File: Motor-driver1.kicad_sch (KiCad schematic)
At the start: 46 parts, among them J8 PINHD_1x4_Male, J9 PINHD_1x4_Male, U2 DRV8825PWP, U3 DRV8825PWP

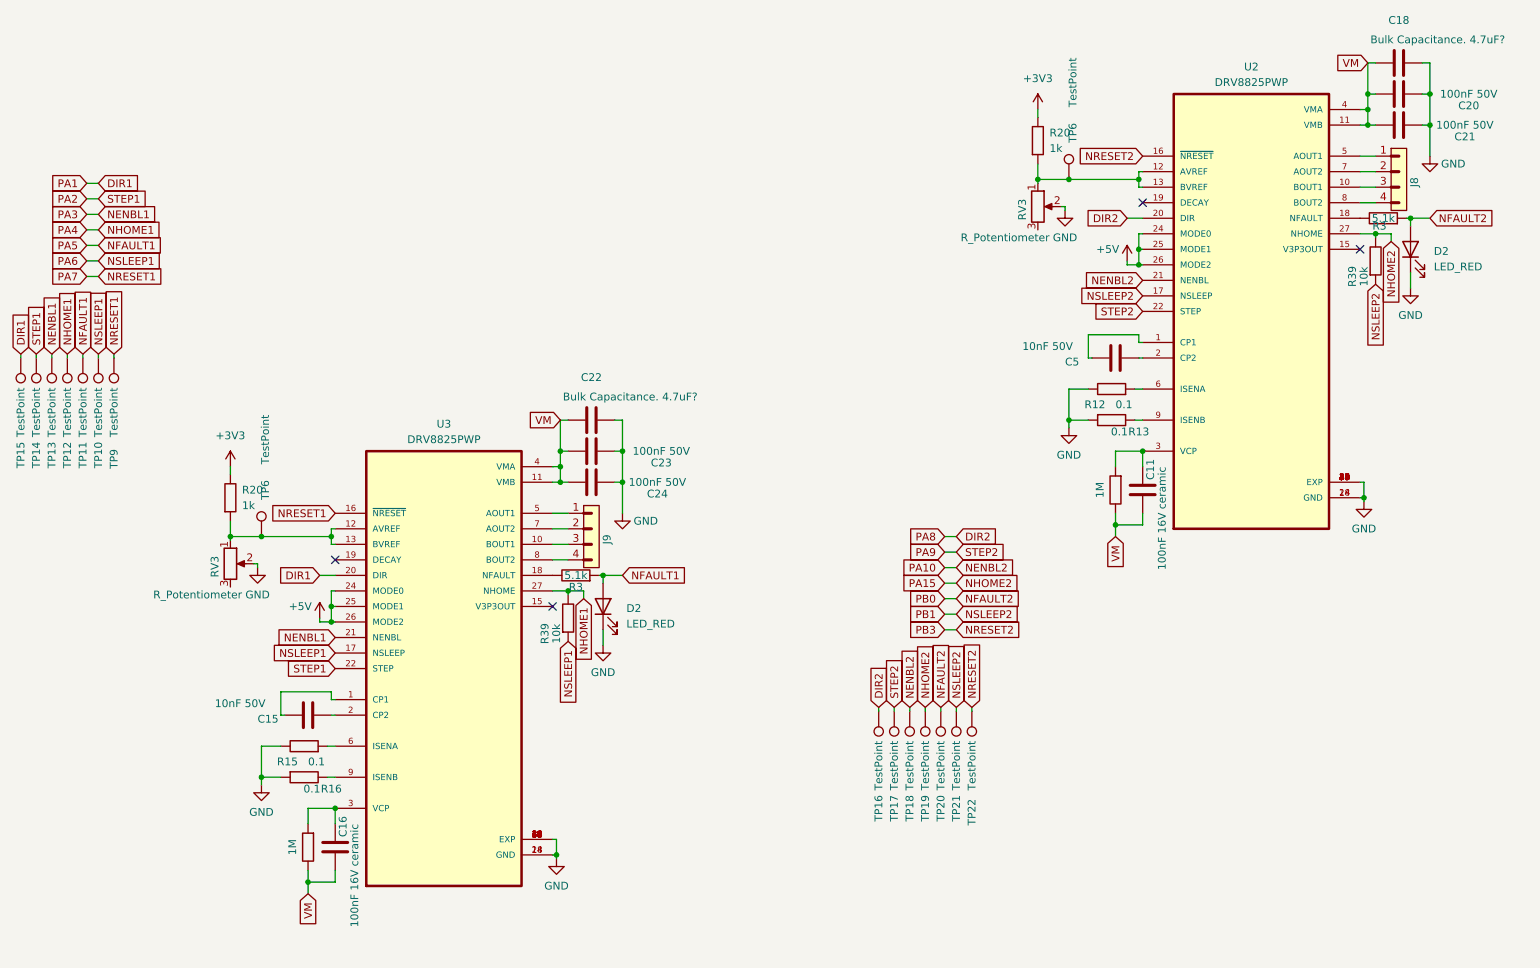
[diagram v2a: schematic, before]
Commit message: routed some paths on schematic. need to rearrange driver pins and come up with solution with motor poer supply
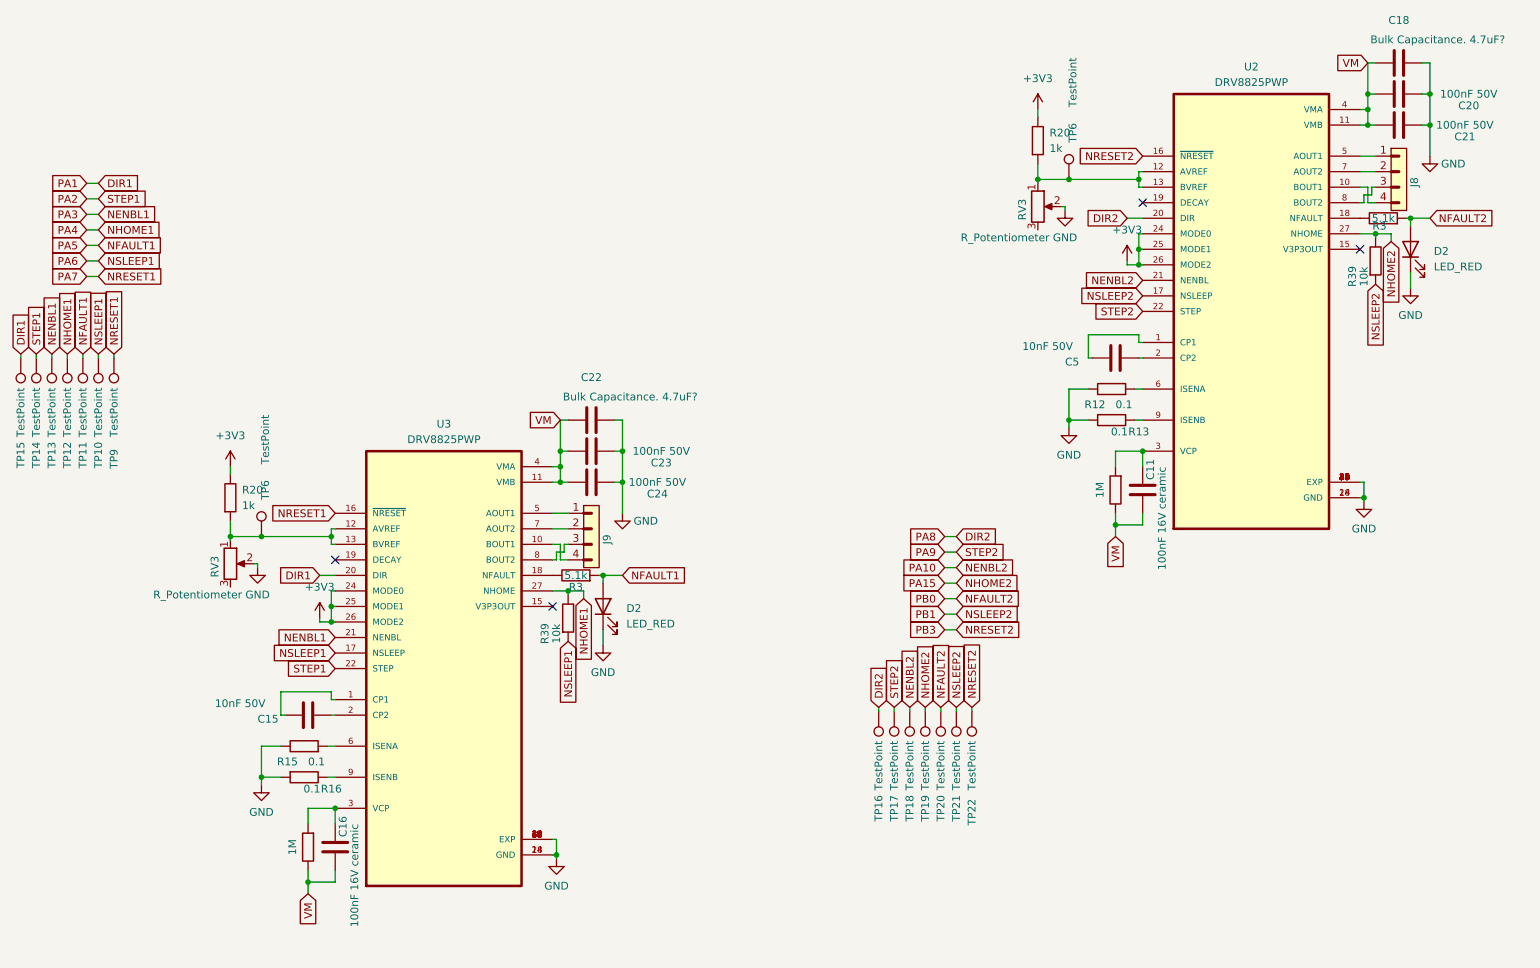
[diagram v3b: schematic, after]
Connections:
- net +5V is gone; now on net +3V3: U2.24 (MODE0), U2.25 (MODE1), U2.26 (MODE2), U3.24 (MODE0), U3.25 (MODE1), U3.26 (MODE2)
- net at J9.3: now also U3.8 (BOUT2); no longer U3.10 (BOUT1)
- net at J9.4: now also U3.10 (BOUT1); no longer U3.8 (BOUT2)
- net at U2.10 (BOUT1): now also J8.4; no longer J8.3
- net at U2.8 (BOUT2): now also J8.3; no longer J8.4
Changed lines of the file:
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@@
+    (stroke (width 0) (type default))
+  )
+  (wire (pts (xy 122.555 113.03) (xy 123.825 113.03))
+    (stroke (width 0) (type default))
+  )
+  (wire (pts (xy 123.825 115.57) (xy 125.095 115.57))
+    (stroke (width 0) (type default))
+  )
+  (wire (pts (xy 124.46 114.3) (xy 124.46 113.03))
     (stroke (width 0) (type default))
   )
@@
     (stroke (width 0) (type default))
   )
-  (wire (pts (xy 257.175 54.61) (xy 254.635 54.61))
-    (stroke (width 0) (type default))
-  )
   (wire (pts (xy 266.065 44.45) (xy 266.065 49.53))
     (stroke (width 0) (type default))
@@
     (stroke (width 0) (type default))
   )
+  (wire (pts (xy 123.19 115.57) (xy 123.19 114.3))
+    (stroke (width 0) (type default))
+  )
   (wire (pts (xy 50.8 82.55) (xy 50.8 81.915))
     (stroke (width 0) (type default))
@@
     (stroke (width 0) (type default))
   )
+  (wire (pts (xy 123.825 113.03) (xy 123.825 115.57))
+    (stroke (width 0) (type default))
+  )
   (wire (pts (xy 82.55 168.275) (xy 82.55 166.37))
     (stroke (width 0) (type default))
@@
     (stroke (width 0) (type default))
   )
+  (wire (pts (xy 124.46 113.03) (xy 125.095 113.03))
+    (stroke (width 0) (type default))
+  )
   (wire (pts (xy 86.995 110.49) (xy 86.36 110.49))
     (stroke (width 0) (type default))
@@
     (stroke (width 0) (type default))
   )
-  (wire (pts (xy 257.175 57.15) (xy 254.635 57.15))
+  (wire (pts (xy 122.555 115.57) (xy 123.19 115.57))
     (stroke (width 0) (type default))
   )
@@
     (stroke (width 0) (type default))
   )
+  (wire (pts (xy 256.54 55.88) (xy 256.54 54.61))
+    (stroke (width 0) (type default))
+  )
+  (wire (pts (xy 255.27 55.88) (xy 256.54 55.88))
+    (stroke (width 0) (type default))
+  )
   (wire (pts (xy 133.985 97.79) (xy 133.985 102.87))
     (stroke (width 0) (type default))
@@
     (stroke (width 0) (type default))
   )
-  (wire (pts (xy 125.095 115.57) (xy 122.555 115.57))
-    (stroke (width 0) (type default))
-  )
   (wire (pts (xy 130.81 118.11) (xy 130.81 119.38))
     (stroke (width 0) (type default))
@@
     (stroke (width 0) (type default))
   )
+  (wire (pts (xy 123.19 114.3) (xy 124.46 114.3))
+    (stroke (width 0) (type default))
+  )
   (wire (pts (xy 255.27 102.87) (xy 254.635 102.87))
     (stroke (width 0) (type default))
@@
     (stroke (width 0) (type default))
   )
+  (wire (pts (xy 255.905 57.15) (xy 257.175 57.15))
+    (stroke (width 0) (type default))
+  )
   (wire (pts (xy 86.36 138.43) (xy 86.36 137.16))
     (stroke (width 0) (type default))
@@
     (stroke (width 0) (type default))
   )
-  (wire (pts (xy 125.095 113.03) (xy 122.555 113.03))
-    (stroke (width 0) (type default))
-  )
   (wire (pts (xy 122.555 120.65) (xy 125.095 120.65))
     (stroke (width 0) (type default))
@@
     (stroke (width 0) (type default))
   )
+  (wire (pts (xy 255.905 54.61) (xy 255.905 57.15))
+    (stroke (width 0) (type default))
+  )
   (wire (pts (xy 218.44 54.61) (xy 219.075 54.61))
     (stroke (width 0) (type default))
@@
     (stroke (width 0) (type default))
   )
+  (wire (pts (xy 254.635 54.61) (xy 255.905 54.61))
+    (stroke (width 0) (type default))
+  )
   (wire (pts (xy 123.19 164.465) (xy 123.19 163.83))
     (stroke (width 0) (type default))
@@
     (stroke (width 0) (type default))
   )
+  (wire (pts (xy 255.27 57.15) (xy 255.27 55.88))
+    (stroke (width 0) (type default))
+  )
   (wire (pts (xy 266.065 59.69) (xy 262.89 59.69))
     (stroke (width 0) (type default))
   )
+  (wire (pts (xy 256.54 54.61) (xy 257.175 54.61))
+    (stroke (width 0) (type default))
+  )
   (wire (pts (xy 186.69 119.38) (xy 188.595 119.38))
     (stroke (width 0) (type default))
@@
   )
   (wire (pts (xy 40.64 82.55) (xy 40.64 81.915))
+    (stroke (width 0) (type default))
+  )
+  (wire (pts (xy 254.635 57.15) (xy 255.27 57.15))
     (stroke (width 0) (type default))
   )
@@
     )
   )
-  (symbol (lib_id "power:+5V") (at 84.455 125.095 0) (unit 1)
-    (in_bom yes) (on_board yes) (dnp no)
-    (property "Reference" "#PWR041" (at 84.455 128.905 0)
-      (effects (font (size 1.27 1.27)) hide)
-    )
-    (property "Value" "+5V" (at 81.28 123.19 0)
-      (effects (font (size 1.27 1.27)))
-    )
-    (property "Footprint" "" (at 84.455 125.095 0)
-      (effects (font (size 1.27 1.27)) hide)
-    )
-    (property "Datasheet" "" (at 84.455 125.095 0)
-      (effects (font (size 1.27 1.27)) hide)
-    )
-    (pin "1")
-    (instances
-      (project "Doodle Drive"
-        (path "/3ec634aa-8c09-482d-9325-2288a4dbd68b/ce40ab82-c304-4dd2-80f5-b6df1964b151"
-          (reference "#PWR041") (unit 1)
-        )
-      )
-    )
-  )
   (symbol (lib_id "Connector:TestPoint") (at 191.135 140.335 180) (unit 1)
     (in_bom yes) (on_board yes) (dnp no)
@@
         (path "/3ec634aa-8c09-482d-9325-2288a4dbd68b/ce40ab82-c304-4dd2-80f5-b6df1964b151"
           (reference "#PWR032") (unit 1)
+        )
+      )
+    )
+  )
+  (symbol (lib_id "power:+3V3") (at 84.455 125.095 0) (unit 1)
+    (in_bom yes) (on_board yes) (dnp no) (fields_autoplaced)
+    (property "Reference" "#PWR041" (at 84.455 128.905 0)
+      (effects (font (size 1.27 1.27)) hide)
+    )
+    (property "Value" "+3V3" (at 84.455 120.015 0)
+      (effects (font (size 1.27 1.27)))
+    )
+    (property "Footprint" "" (at 84.455 125.095 0)
+      (effects (font (size 1.27 1.27)) hide)
+    )
+    (property "Datasheet" "" (at 84.455 125.095 0)
+      (effects (font (size 1.27 1.27)) hide)
+    )
+    (pin "1")
+    (instances
+      (project "Doodle Drive"
+        (path "/3ec634aa-8c09-482d-9325-2288a4dbd68b/ce40ab82-c304-4dd2-80f5-b6df1964b151"
+          (reference "#PWR041") (unit 1)
         )
       )
@@
     )
   )
-  (symbol (lib_id "power:+5V") (at 216.535 66.675 0) (unit 1)
-    (in_bom yes) (on_board yes) (dnp no)
-    (property "Reference" "#PWR039" (at 216.535 70.485 0)
-      (effects (font (size 1.27 1.27)) hide)
-    )
-    (property "Value" "+5V" (at 213.36 64.77 0)
-      (effects (font (size 1.27 1.27)))
-    )
-    (property "Footprint" "" (at 216.535 66.675 0)
-      (effects (font (size 1.27 1.27)) hide)
-    )
-    (property "Datasheet" "" (at 216.535 66.675 0)
-      (effects (font (size 1.27 1.27)) hide)
-    )
-    (pin "1")
-    (instances
-      (project "Doodle Drive"
-        (path "/3ec634aa-8c09-482d-9325-2288a4dbd68b/ce40ab82-c304-4dd2-80f5-b6df1964b151"
-          (reference "#PWR039") (unit 1)
-        )
-      )
-    )
-  )
   (symbol (lib_id "Device:C") (at 128.905 97.79 90) (unit 1)
     (in_bom yes) (on_board yes) (dnp no)
@@
         )
       )
+    )
+  )
+  (symbol (lib_id "power:+3V3") (at 216.535 66.675 0) (unit 1)
+    (in_bom yes) (on_board yes) (dnp no) (fields_autoplaced)
+    (property "Reference" "#PWR039" (at 216.535 70.485 0)
+      (effects (font (size 1.27 1.27)) hide)
+    )
+    (property "Value" "+3V3" (at 216.535 61.595 0)
+      (effects (font (size 1.27 1.27)))
+    )
+    (property "Footprint" "" (at 216.535 66.675 0)
+      (effects (font (size 1.27 1.27)) hide)
+    )
+    (property "Datasheet" "" (at 216.535 66.675 0)
+      (effects (font (size 1.27 1.27)) hide)
+    )
+    (pin "1")
+    (instances
+      (project "Doodle Drive"
+        (path "/3ec634aa-8c09-482d-9325-2288a4dbd68b/ce40ab82-c304-4dd2-80f5-b6df1964b151"
+          (reference "#PWR039") (unit 1)
+        )
+      )

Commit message: temporarly detached testpoints
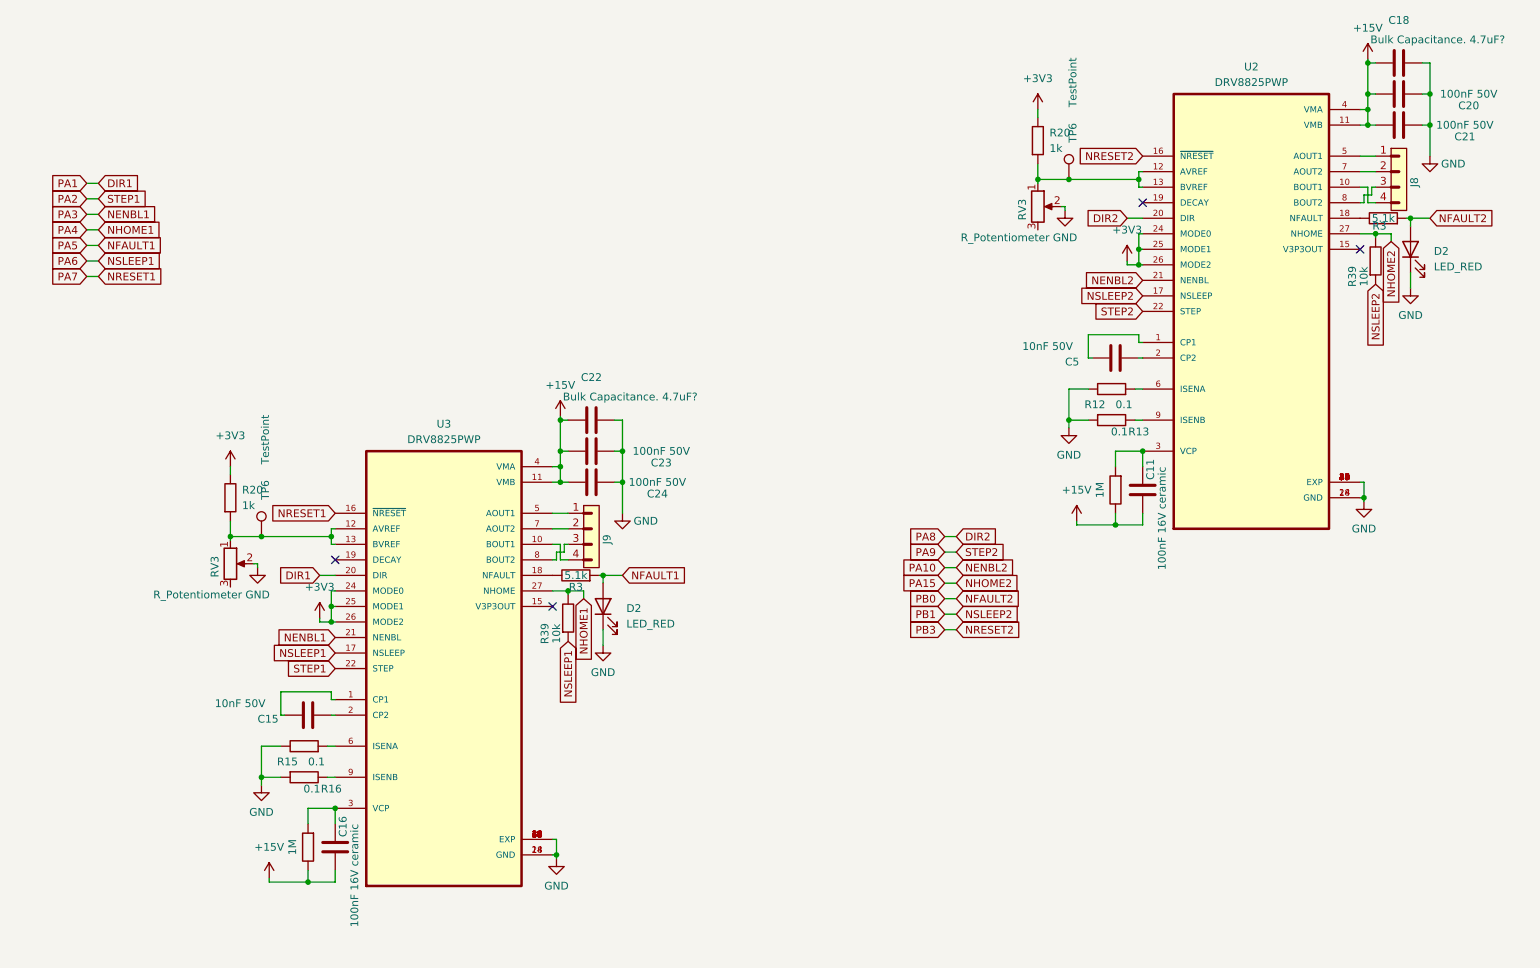
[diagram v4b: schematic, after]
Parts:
- removed TP10, TP11, TP12, TP13, TP14, TP15, TP16, TP17, TP18, TP19, TP20, TP21, TP22, TP9: TestPoint, TestPoint:TestPoint_Pad_D2.5mm, symbol Connector:TestPoint
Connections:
- net VM renamed +15V

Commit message: routet Motor Driver modules, reattached and placed testpoints
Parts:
- C11, C16: footprint Capacitor_SMD:C_01005_0402Metric -> Capacitor_SMD:C_0402_1005Metric
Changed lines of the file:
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@@
       (effects (font (size 1.27 1.27)) (justify left))
     )
-    (property "Footprint" "Capacitor_SMD:C_01005_0402Metric" (at 86.0298 158.75 0)
+    (property "Footprint" "Capacitor_SMD:C_0402_1005Metric" (at 86.0298 158.75 0)
       (effects (font (size 1.27 1.27)) hide)
     )
@@
       (effects (font (size 1.27 1.27)) (justify left))
     )
-    (property "Footprint" "Capacitor_SMD:C_01005_0402Metric" (at 218.1098 100.33 0)
-      (effects (font (size 1.27 1.27)) hide)
-    )
+    (property "Footprint" "Capacitor_SMD:C_0402_1005Metric" (at 218.1098 100.33 0)
+      (effects (font (size 1.27 1.27)) hide)
+    )
